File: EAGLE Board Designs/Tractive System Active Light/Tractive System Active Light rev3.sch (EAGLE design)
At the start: 29 parts, among them X2 MAIN

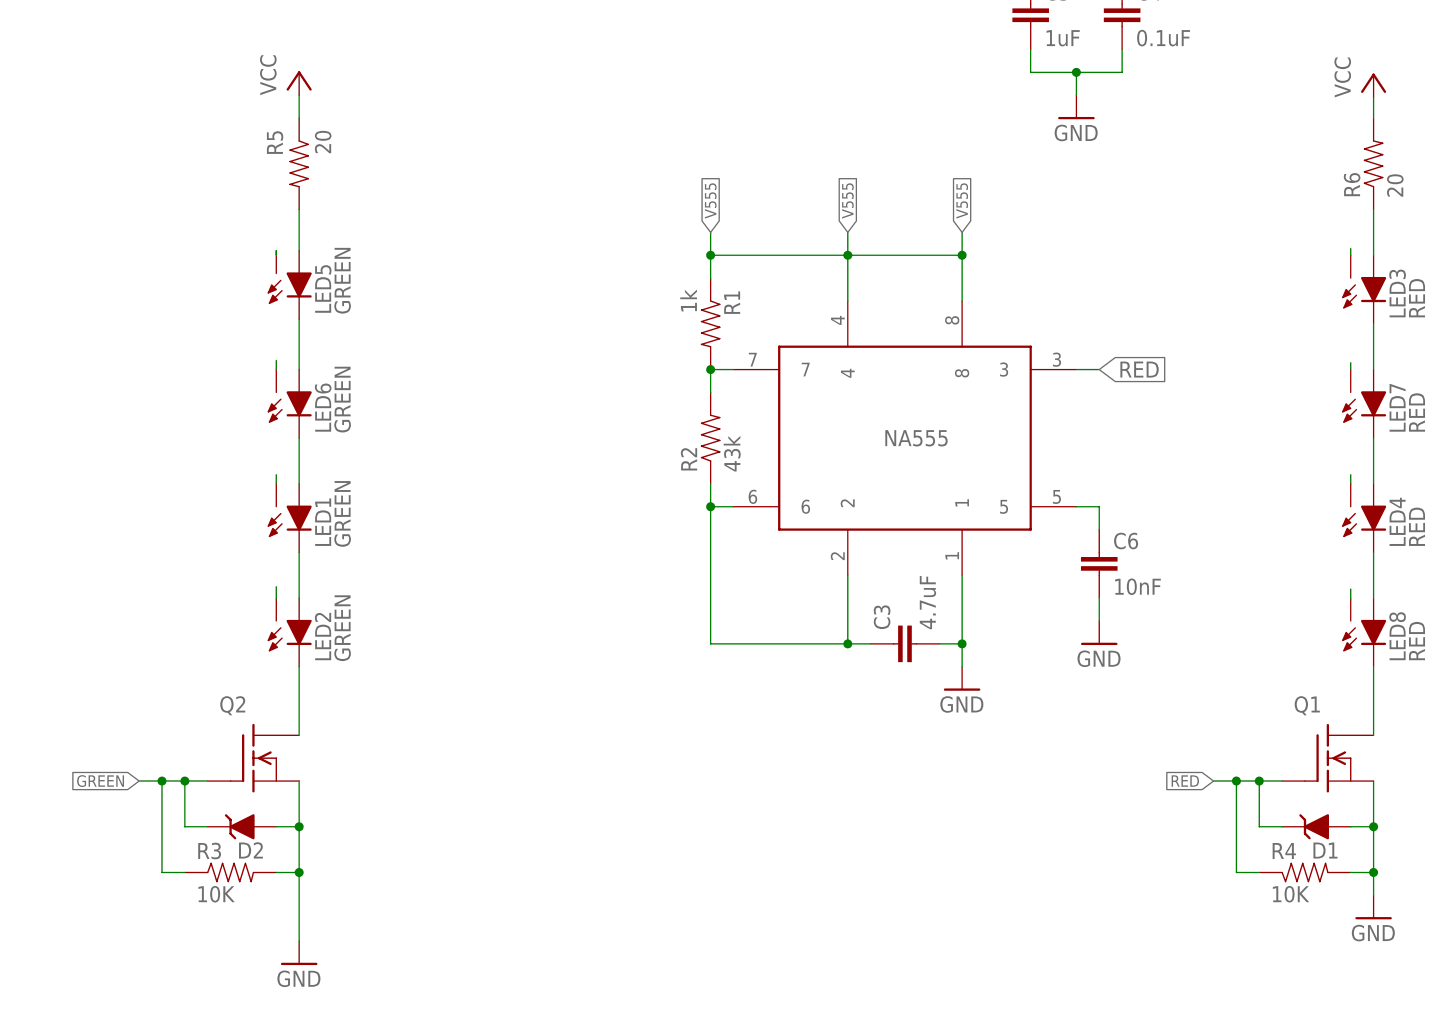
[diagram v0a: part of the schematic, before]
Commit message: added the new na555 timer schematic
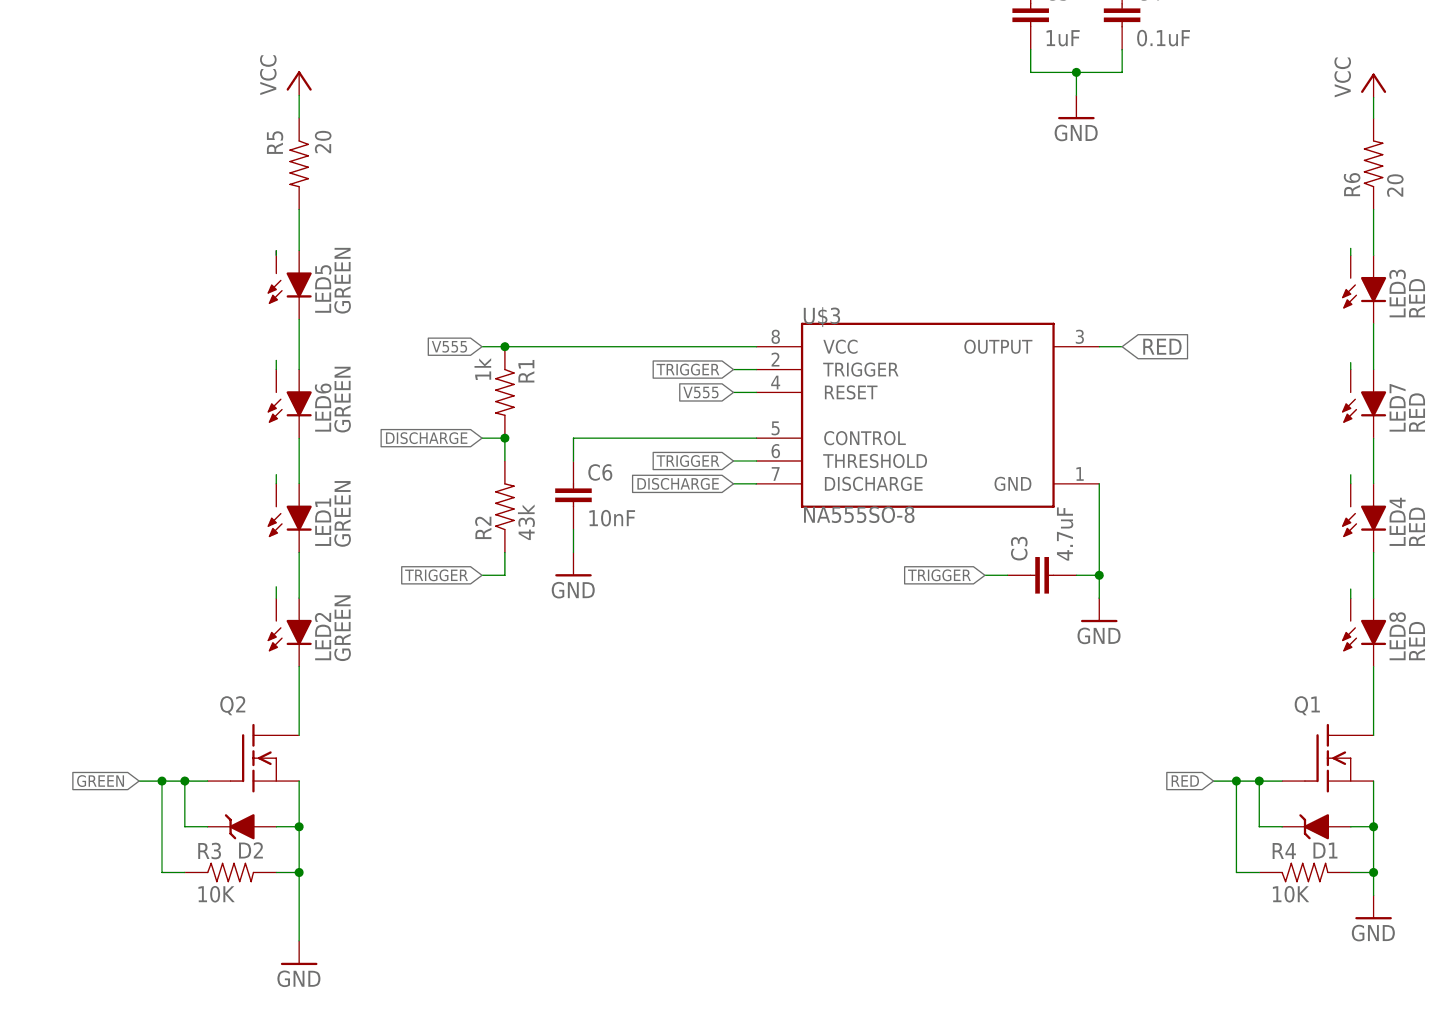
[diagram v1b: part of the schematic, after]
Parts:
- removed NA555: NA555SO-8, HyTechDevices:NA555SO-8
- added U$3: NA555SO-8, HyTechDevices:NA555SO-8
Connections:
- removed net N$8: C3.1, NA555.2, NA555.6, R2.1
- removed net N$9: NA555.7, R1.2, R2.2
- new net DISCHARGE: R1.2, R2.2, U$3.DISCHARGE
- new net TRIGGER: C3.1, R2.1, U$3.THRESHOLD, U$3.TRIGGER
- net GND: now also U$3.GND; no longer NA555.1
- net N$13: now also U$3.CONTROL; no longer NA555.5
- net RED: now also U$3.OUTPUT; no longer NA555.3
- net V555: now also U$3.RESET, U$3.VCC; no longer NA555.4, NA555.8
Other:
- moved on the sheet: C3, C6, R1, R2

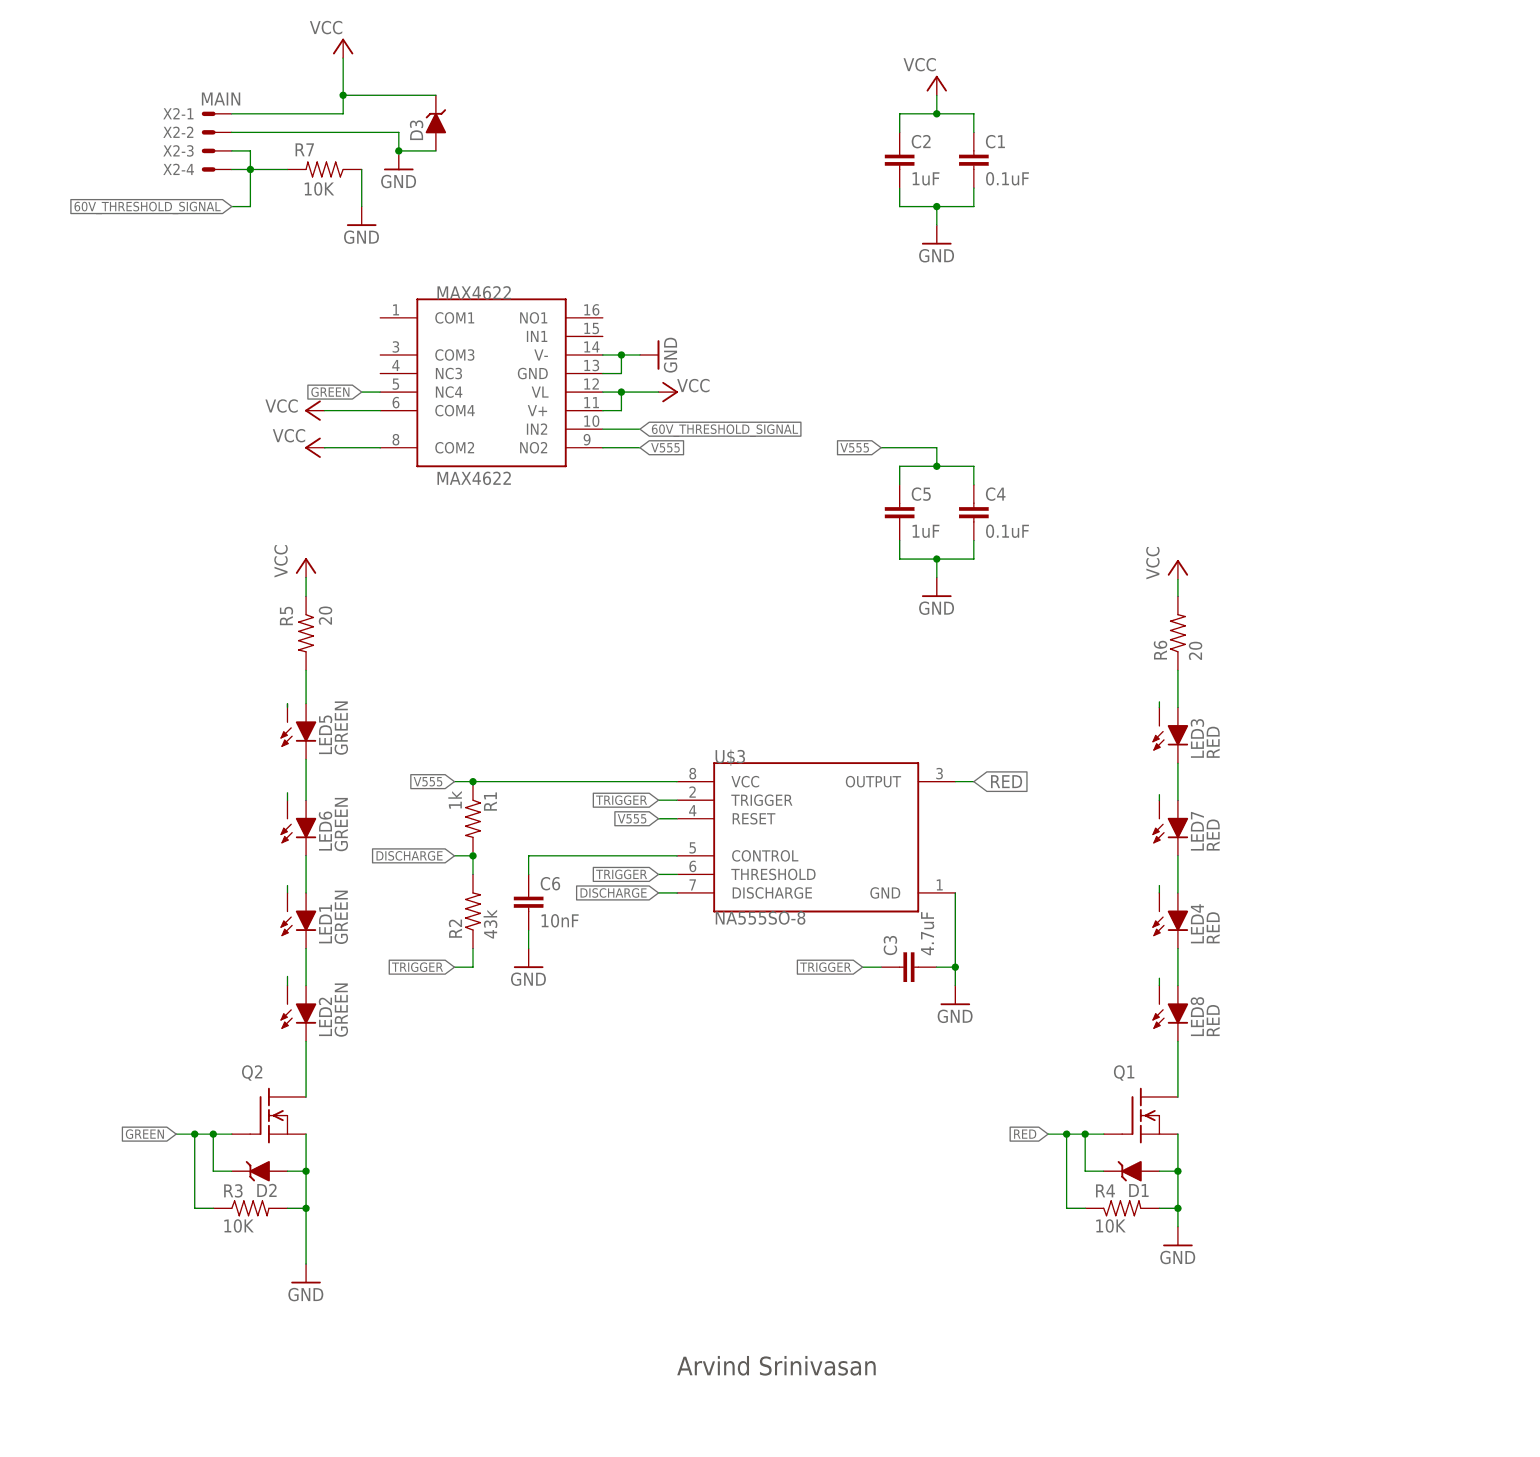
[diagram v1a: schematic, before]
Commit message: Added the gate resistor and made the text on the symbols layer
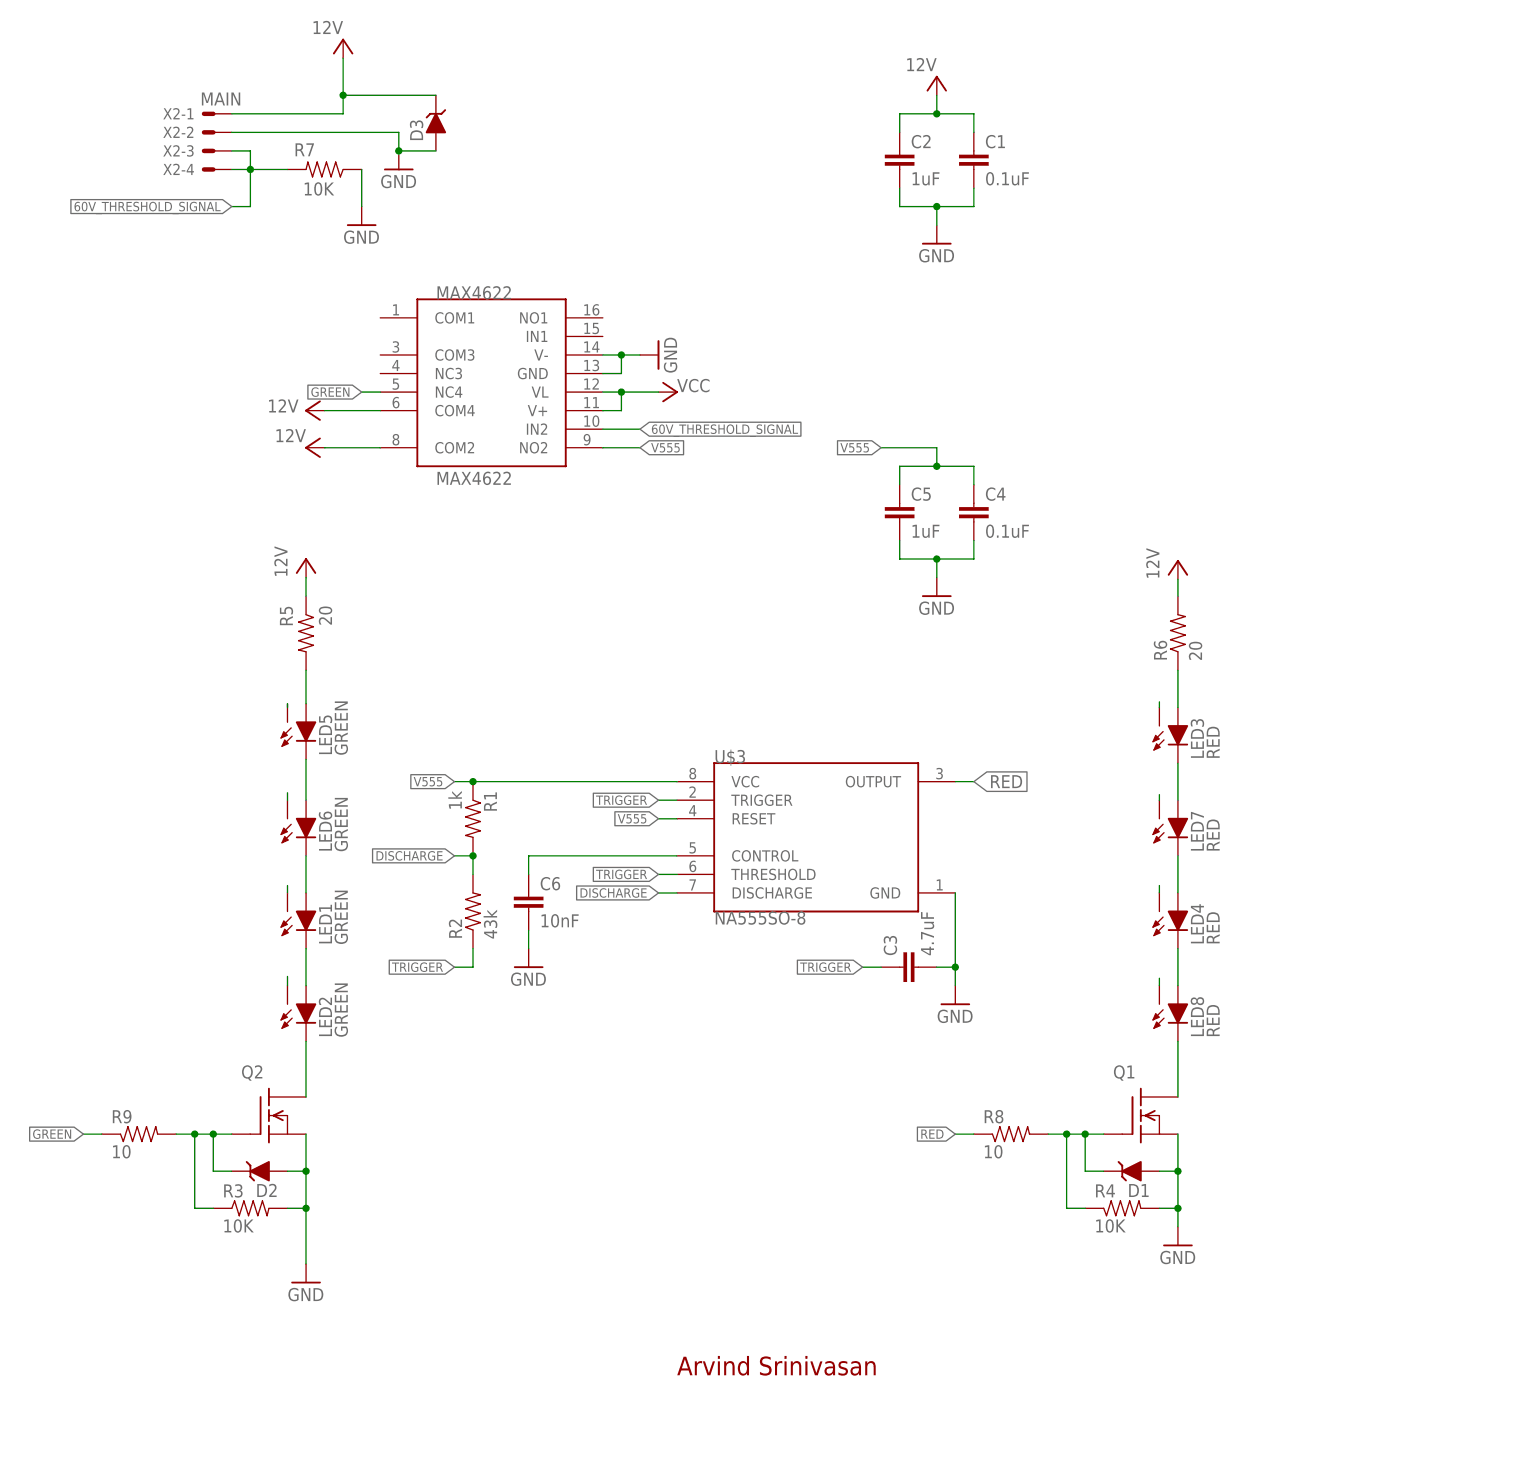
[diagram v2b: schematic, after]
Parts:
- added R8, R9: 10, HyTechDevices:RESISTOR0603-RES
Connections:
- new net N$4: D1.C, Q1.G, R4.1, R8.2
- new net N$6: D2.C, Q2.G, R3.1, R9.2
- net GREEN: now also R9.1; no longer D2.C, Q2.G, R3.1
- net RED: now also R8.1; no longer D1.C, Q1.G, R4.1

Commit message: Added a description to the schematic
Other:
- note added: "TSAL Rev 3 Schematic"
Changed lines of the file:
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@@
 <plain>
 <text x="20.32" y="-60.96" size="2.54" layer="94">Arvind Srinivasan</text>
+<text x="91.44" y="-68.58" size="2.54" layer="94">TSAL Rev 3 Schematic</text>
 </plain>
 <instances>

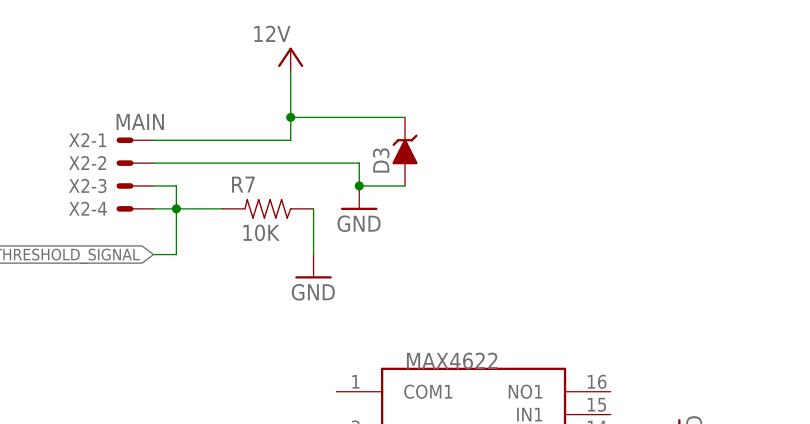
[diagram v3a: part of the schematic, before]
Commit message: Changed a zener diode to a tvs diode and got rid of the LED silkscreen
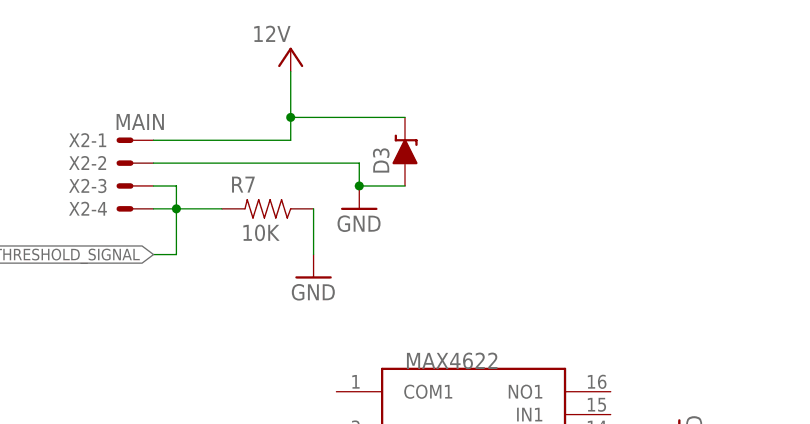
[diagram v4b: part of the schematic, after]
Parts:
- D3: device HyTechDevices:DIODE_ZENER0603 -> HyTechDevices:TVS_DIODE
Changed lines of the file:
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@@
 <part name="GND1" library="HyTechSymbols" deviceset="GND" device=""/>
 <part name="U$1" library="HyTechFrames" deviceset="FRAME_A_L" device=""/>
-<part name="D3" library="HyTechDevices" deviceset="DIODE_ZENER" device="0603" value="D15V0S1U2LP1608"/>
+<part name="D3" library="HyTechDevices" deviceset="TVS_DIODE" device="" value="D15V0S1U2LP1608"/>
 <part name="D2" library="HyTechDevices" deviceset="DIODE_ZENER" device="" value="MMBZ5246BLT1G"/>
 <part name="D1" library="HyTechDevices" deviceset="DIODE_ZENER" device="" value="MMBZ5246BLT1G"/>
